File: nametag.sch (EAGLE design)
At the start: 23 parts, among them U1 MCP73831

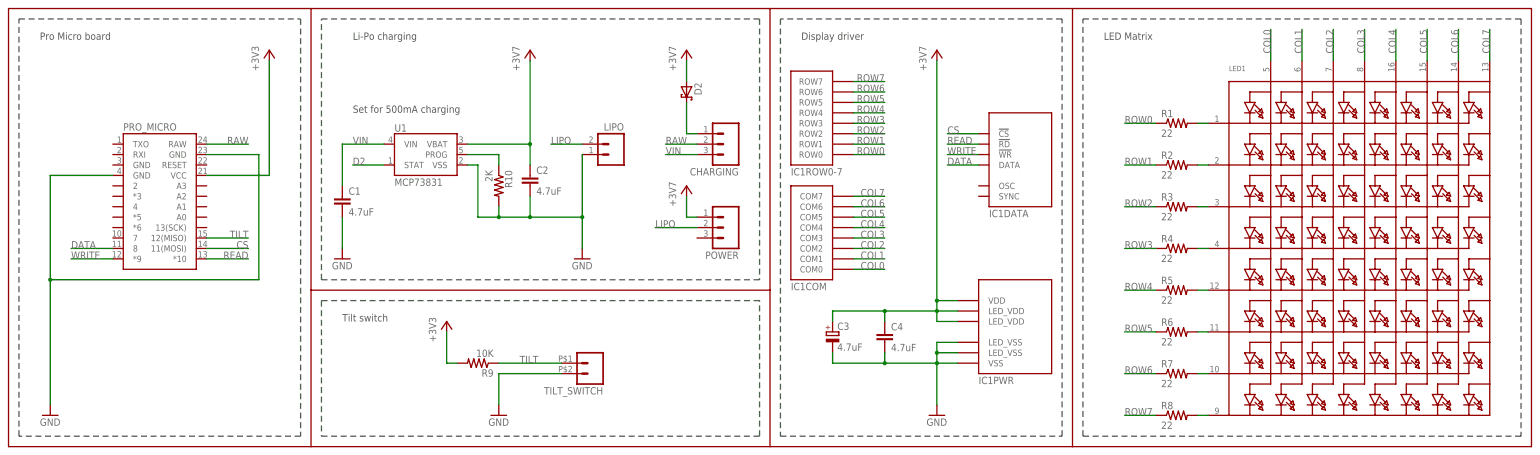
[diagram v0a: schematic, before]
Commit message: separated battery and microcontroller VCC
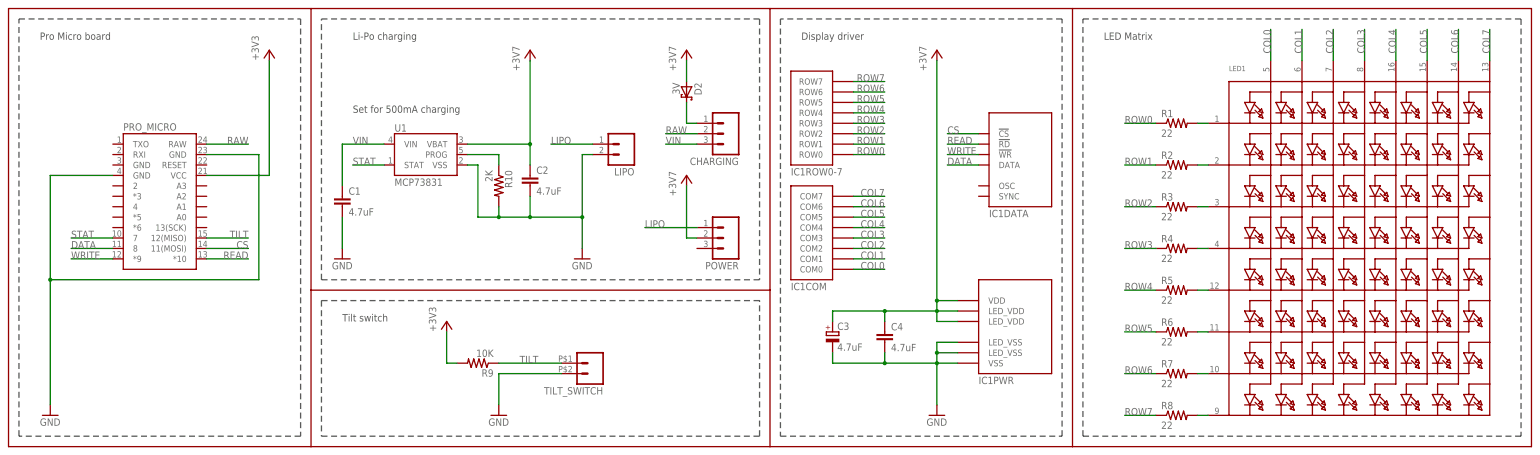
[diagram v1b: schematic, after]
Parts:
- D2: value BAT60J -> 3V
- LIPO: value LiPo Battery -> M02JST-PTH-VERT
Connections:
- removed net D2: U1.STAT
- new net STAT: PRO_MICRO.7, U1.STAT
- new net VCC: PRO_MICRO.VCC, R9.2
- net +3V3: now also POWER.2; no longer POWER.1, PRO_MICRO.VCC, R9.2
- net GND: now also LIPO.2; no longer LIPO.1
- net LIPO: now also LIPO.1, POWER.1; no longer LIPO.2, POWER.2
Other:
- moved on the sheet: CHARGING, LIPO, POWER
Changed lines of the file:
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@@
 <part name="C1" library="SparkFun" deviceset="CAP" device="0402-CAP" value="4.7uF"/>
 <part name="C2" library="SparkFun" deviceset="CAP" device="0402-CAP" value="4.7uF"/>
-<part name="LIPO" library="SparkFun-Connectors" deviceset="M02" device="JST-PTH-VERT" value="LiPo Battery"/>
 <part name="GND2" library="SparkFun" deviceset="GND" device=""/>
 <part name="LED1" library="adafruit" deviceset="SEGMENT_8X8_ROWCATHODE" device=""/>
@@
 <part name="+3V7" library="supply1" deviceset="+3V3" device="" value="+3V7"/>
 <part name="CHARGING" library="SparkFun-Connectors" deviceset="M03" device="PTH"/>
-<part name="D2" library="diode" deviceset="BAT60J" device="" value=""/>
+<part name="D2" library="diode" deviceset="BAT60J" device="" value="3V"/>
 <part name="+3V1" library="supply1" deviceset="+3V3" device="" value="+3V7"/>
 <part name="+3V2" library="supply1" deviceset="+3V3" device="" value="+3V7"/>
@@
 <part name="TILT_SWITCH" library="SparkFun-Connectors" deviceset="M02" device="PTH2" value=""/>
 <part name="R9" library="SparkFun" deviceset="RESISTOR" device="0402-RES" value="10K"/>
-<part name="+3V3" library="supply1" deviceset="+3V3" device=""/>
-<part name="+3V4" library="supply1" deviceset="+3V3" device=""/>
 <part name="GND4" library="SparkFun" deviceset="GND" device=""/>
 <part name="POWER" library="SparkFun-Connectors" deviceset="M03" device="PTH"/>
 <part name="+3V5" library="supply1" deviceset="+3V3" device="" value="+3V7"/>
+<part name="LIPO" library="SparkFun-Connectors" deviceset="M02" device="JST-PTH-VERT" value=""/>
+<part name="P+1" library="supply1" deviceset="VCC" device="" value="+3V3"/>
+<part name="P+2" library="supply1" deviceset="VCC" device="" value="+3V3"/>
 </parts>
 <sheets>
@@
 <instance part="C1" gate="G$1" x="81.28" y="58.42"/>
 <instance part="C2" gate="G$1" x="127" y="63.5"/>
-<instance part="LIPO" gate="G$1" x="147.32" y="71.12" smashed="yes" rot="MR0">
-<attribute name="NAME" x="149.86" y="76.962" size="1.778" layer="95" rot="MR0"/>
-</instance>
 <instance part="GND2" gate="1" x="139.7" y="45.72"/>
 <instance part="LED1" gate="G$1" x="330.2" y="45.72"/>
@@
 <instance part="GND1" gate="1" x="10.16" y="7.62"/>
 <instance part="+3V7" gate="G$1" x="127" y="96.52"/>
-<instance part="CHARGING" gate="G$1" x="175.26" y="73.66" rot="R180"/>
+<instance part="CHARGING" gate="G$1" x="175.26" y="76.2" rot="R180"/>
 <instance part="D2" gate="G$1" x="165.1" y="86.36" rot="R270"/>
 <instance part="+3V1" gate="G$1" x="165.1" y="96.52"/>
@@
 <instance part="TILT_SWITCH" gate="G$1" x="142.24" y="20.32" rot="R180"/>
 <instance part="R9" gate="G$1" x="114.3" y="20.32" rot="R180"/>
-<instance part="+3V3" gate="G$1" x="63.5" y="96.52"/>
-<instance part="+3V4" gate="G$1" x="106.68" y="30.48"/>
 <instance part="GND4" gate="1" x="119.38" y="7.62"/>
-<instance part="POWER" gate="G$1" x="175.26" y="53.34" rot="R180"/>
-<instance part="+3V5" gate="G$1" x="165.1" y="63.5"/>
+<instance part="POWER" gate="G$1" x="175.26" y="50.8" rot="R180"/>
+<instance part="+3V5" gate="G$1" x="165.1" y="66.04"/>
+<instance part="LIPO" gate="G$1" x="149.86" y="73.66" rot="R180"/>
+<instance part="P+1" gate="VCC" x="106.68" y="30.48"/>
+<instance part="P+2" gate="VCC" x="63.5" y="96.52"/>
 </instances>
 <busses>
@@
 <wire x1="127" y1="55.88" x2="127" y2="60.96" width="0.1524" layer="91"/>
 <wire x1="119.38" y1="55.88" x2="127" y2="55.88" width="0.1524" layer="91"/>
+<wire x1="142.24" y1="71.12" x2="139.7" y2="71.12" width="0.1524" layer="91"/>
 <wire x1="139.7" y1="71.12" x2="139.7" y2="55.88" width="0.1524" layer="91"/>
-<pinref part="LIPO" gate="G$1" pin="1"/>
 <wire x1="127" y1="55.88" x2="139.7" y2="55.88" width="0.1524" layer="91"/>
 <pinref part="GND2" gate="1" pin="GND"/>
@@
 <junction x="127" y="55.88"/>
 <junction x="139.7" y="55.88"/>
+<pinref part="LIPO" gate="G$1" pin="2"/>
 </segment>
 <segment>
@@
 <segment>
 <pinref part="CHARGING" gate="G$1" pin="3"/>
-<wire x1="167.64" y1="71.12" x2="160.02" y2="71.12" width="0.1524" layer="91"/>
-<label x="160.02" y="71.12" size="1.778" layer="95"/>
+<wire x1="167.64" y1="73.66" x2="160.02" y2="73.66" width="0.1524" layer="91"/>
+<label x="160.02" y="73.66" size="1.778" layer="95"/>
 </segment>
 </net>
@@
 <wire x1="48.26" y1="48.26" x2="58.42" y2="48.26" width="0.1524" layer="91"/>
 <label x="58.42" y="48.26" size="1.778" layer="95" rot="MR0"/>
-</segment>
-</net>
-<net name="D2" class="0">
-<segment>
-<wire x1="91.44" y1="68.58" x2="83.82" y2="68.58" width="0.1524" layer="91"/>
-<pinref part="U1" gate="G$1" pin="STAT"/>
-<label x="83.82" y="68.58" size="1.778" layer="95"/>
 </segment>
 </net>
@@
 </segment>
 <segment>
-<pinref part="PRO_MICRO" gate="G$1" pin="VCC"/>
-<pinref part="+3V3" gate="G$1" pin="+3V3"/>
-<wire x1="48.26" y1="66.04" x2="63.5" y2="66.04" width="0.1524" layer="91"/>
-<wire x1="63.5" y1="66.04" x2="63.5" y2="93.98" width="0.1524" layer="91"/>
-</segment>
-<segment>
-<pinref part="R9" gate="G$1" pin="2"/>
-<pinref part="+3V4" gate="G$1" pin="+3V3"/>
-<wire x1="109.22" y1="20.32" x2="106.68" y2="20.32" width="0.1524" layer="91"/>
-<wire x1="106.68" y1="20.32" x2="106.68" y2="27.94" width="0.1524" layer="91"/>
-</segment>
-<segment>
-<pinref part="POWER" gate="G$1" pin="1"/>
+<pinref part="POWER" gate="G$1" pin="2"/>
 <pinref part="+3V5" gate="G$1" pin="+3V3"/>
-<wire x1="167.64" y1="55.88" x2="165.1" y2="55.88" width="0.1524" layer="91"/>
-<wire x1="165.1" y1="55.88" x2="165.1" y2="60.96" width="0.1524" layer="91"/>
+<wire x1="167.64" y1="50.8" x2="165.1" y2="50.8" width="0.1524" layer="91"/>
+<wire x1="165.1" y1="50.8" x2="165.1" y2="63.5" width="0.1524" layer="91"/>
 </segment>
 </net>
@@
 <segment>
 <pinref part="CHARGING" gate="G$1" pin="2"/>
-<wire x1="167.64" y1="73.66" x2="160.02" y2="73.66" width="0.1524" layer="91"/>
-<label x="160.02" y="73.66" size="1.778" layer="95"/>
+<wire x1="167.64" y1="76.2" x2="160.02" y2="76.2" width="0.1524" layer="91"/>
+<label x="160.02" y="76.2" size="1.778" layer="95"/>
 </segment>
 <segment>
@@
 <pinref part="CHARGING" gate="G$1" pin="1"/>
 <pinref part="D2" gate="G$1" pin="C"/>
-<wire x1="167.64" y1="76.2" x2="165.1" y2="76.2" width="0.1524" layer="91"/>
-<wire x1="165.1" y1="76.2" x2="165.1" y2="83.82" width="0.1524" layer="91"/>
+<wire x1="167.64" y1="78.74" x2="165.1" y2="78.74" width="0.1524" layer="91"/>
+<wire x1="165.1" y1="78.74" x2="165.1" y2="83.82" width="0.1524" layer="91"/>
 </segment>
 </net>
@@
 <net name="LIPO" class="0">
 <segment>
-<pinref part="LIPO" gate="G$1" pin="2"/>
-<wire x1="139.7" y1="73.66" x2="134.62" y2="73.66" width="0.1524" layer="91"/>
-<wire x1="132.08" y1="73.66" x2="134.62" y2="73.66" width="0.1524" layer="91"/>
+<wire x1="142.24" y1="73.66" x2="132.08" y2="73.66" width="0.1524" layer="91"/>
 <label x="132.08" y="73.66" size="1.778" layer="95"/>
-</segment>
-<segment>
-<pinref part="POWER" gate="G$1" pin="2"/>
-<wire x1="167.64" y1="53.34" x2="157.48" y2="53.34" width="0.1524" layer="91"/>
-<label x="157.48" y="53.34" size="1.778" layer="95"/>
-</segment>
-</net>
+<pinref part="LIPO" gate="G$1" pin="1"/>
+</segment>
+<segment>
+<pinref part="POWER" gate="G$1" pin="1"/>
+<wire x1="167.64" y1="53.34" x2="154.94" y2="53.34" width="0.1524" layer="91"/>
+<label x="154.94" y="53.34" size="1.778" layer="95"/>
+</segment>
+</net>
+<net name="STAT" class="0">
+<segment>
+<pinref part="PRO_MICRO" gate="G$1" pin="7"/>
+<wire x1="25.4" y1="50.8" x2="15.24" y2="50.8" width="0.1524" layer="91"/>
+<label x="15.24" y="50.8" size="1.778" layer="95"/>
+</segment>
+<segment>
+<wire x1="91.44" y1="68.58" x2="83.82" y2="68.58" width="0.1524" layer="91"/>
+<pinref part="U1" gate="G$1" pin="STAT"/>
+<label x="83.82" y="68.58" size="1.778" layer="95"/>
+</segment>
+</net>
+<net name="VCC" class="0">
+<segment>
+<pinref part="R9" gate="G$1" pin="2"/>
+<wire x1="109.22" y1="20.32" x2="106.68" y2="20.32" width="0.1524" layer="91"/>
+<wire x1="106.68" y1="20.32" x2="106.68" y2="27.94" width="0.1524" layer="91"/>
+<pinref part="P+1" gate="VCC" pin="VCC"/>
+</segment>
+<segment>
+<pinref part="PRO_MICRO" gate="G$1" pin="VCC"/>
+<wire x1="48.26" y1="66.04" x2="63.5" y2="66.04" width="0.1524" layer="91"/>
+<wire x1="63.5" y1="66.04" x2="63.5" y2="93.98" width="0.1524" layer="91"/>
+<pinref part="P+2" gate="VCC" pin="VCC"/>
+</segment>
+</net>

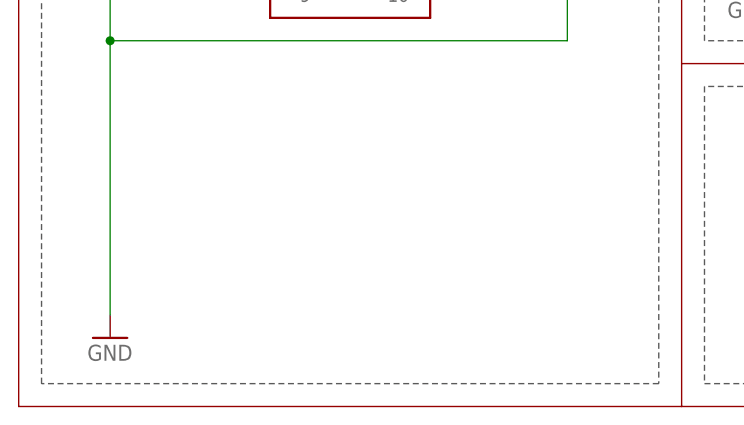
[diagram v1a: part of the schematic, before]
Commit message: updated logos
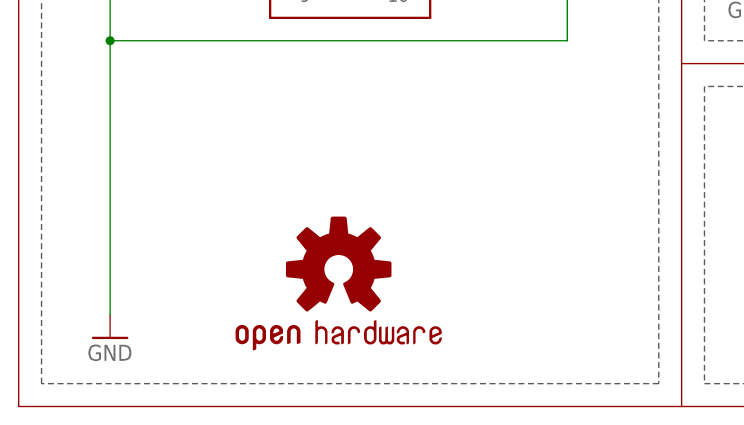
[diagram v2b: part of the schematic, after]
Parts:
- added LOGO1: OSHW-LOGOS, SparkFun-Aesthetics:OSHW-LOGOS
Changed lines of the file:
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@@
 <part name="P+1" library="supply1" deviceset="VCC" device="" value="+3V3"/>
 <part name="P+2" library="supply1" deviceset="VCC" device="" value="+3V3"/>
+<part name="LOGO1" library="SparkFun-Aesthetics" deviceset="OSHW-LOGO" device="S" value="OSHW-LOGOS"/>
 </parts>
 <sheets>
@@
 <instance part="P+1" gate="VCC" x="106.68" y="30.48"/>
 <instance part="P+2" gate="VCC" x="63.5" y="96.52"/>
+<instance part="LOGO1" gate="G$1" x="35.56" y="15.24"/>
 </instances>
 <busses>

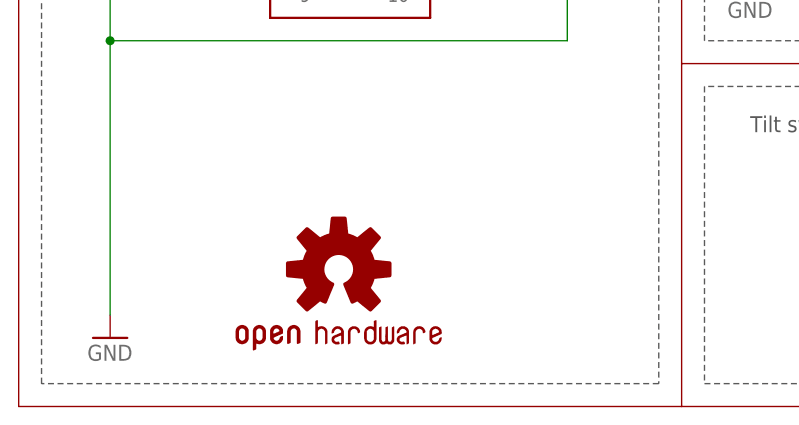
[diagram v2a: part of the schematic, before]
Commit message: updated nametag schematic and board
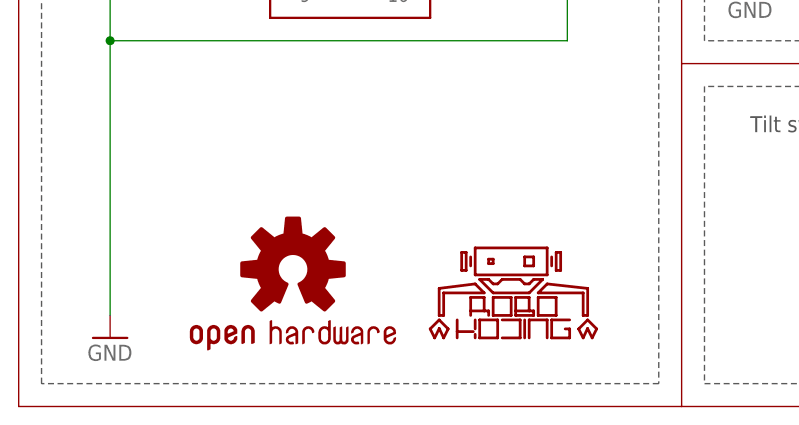
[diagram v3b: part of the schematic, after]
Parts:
- added LOGO2: ROBOKODING-LOGOS, Sumorobot:ROBOKODING-LOGOS
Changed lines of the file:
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@@
 <part name="P+2" library="supply1" deviceset="VCC" device="" value="+3V3"/>
 <part name="LOGO1" library="SparkFun-Aesthetics" deviceset="OSHW-LOGO" device="S" value="OSHW-LOGOS"/>
+<part name="LOGO2" library="Sumorobot" deviceset="ROBOKODING-LOGO" device="S"/>
 </parts>
 <sheets>
@@
 <instance part="P+1" gate="VCC" x="106.68" y="30.48"/>
 <instance part="P+2" gate="VCC" x="63.5" y="96.52"/>
-<instance part="LOGO1" gate="G$1" x="35.56" y="15.24"/>
+<instance part="LOGO1" gate="G$1" x="30.48" y="15.24"/>
+<instance part="LOGO2" gate="G$1" x="45.72" y="7.62"/>
 </instances>
 <busses>
